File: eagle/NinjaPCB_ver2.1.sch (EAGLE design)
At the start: 58 parts, among them IC3 ANALOGSW_AD_SOT23-6, IC6 NAU7802, J2 ATX24, J3 HEATER, J4 HEATER_TEMP, Q1 S8550, Q2 IRF520NPBF, Q3 IRF520NPBF, Q4 S8550, Q5 IRF520NPBF, Q6 S8550, Q7 S8550, Q8 S8550, U1 CJT1117-3.3-SOT223

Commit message: set default 4x4
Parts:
- removed C7: CAP_SMDAL_1000UF_25V, Seeed-OPL-2017-01-Capacitor-akita:CAP_SMDAL_1000UF_25V
- removed ESP1: ESP-12F, Seeed-OPL-2017-01-Sensor-camilo:ESP-12F
- removed ESP2: ESP-WROOM-02-BREAK, PCR-Module:ESP-WROOM-02-BREAK
- removed IC3: ANALOGSW_AD_SOT23-6, PCR-IC:ANALOGSW_AD_SOT23-6
- removed IC6: NAU7802, PCR-IC:NAU7802
- removed J2: ATX24, PCR-Connector:ATX24
- removed J4: HEATER_TEMP, Seeed-Connector:SCREW-TERMINAL-GREEN(2P-3.5)
- removed JP2: 22-23-2031, con-molex:22-23-2031
- removed PWR: (no value), pinhead:PINHD-1X2
- removed Q7, Q8: S8550, Seeed-Transistor:SMD-TRANSISTORS-PNP-25V-500MA-S8550(SOT-23)
- removed R20: 100K 1/10W, Seeed-Resistor:SMD-RES-100K-5%-1/10W(0603)
- removed R22: 10K 1/10W, Seeed-Resistor:SMD-RES-10K-5%-1/10W(0603)
- removed RH1, RH2, RL: 30K HP, PCR-RCL:R0603
- removed SERIAL: (no value), pinhead:PINHD-1X6
- removed U1: CJT1117-3.3-SOT223, Seeed-IC:PMIC-CJT1117-3.3(SOT223)
- added ATX: ATX24NH, PCR-Connector:ATX24NH
- added C4: 22uf, Seeed-Capacitor:TANTALUM-SMD-22UF-16V(AVX-B)
- added CP1, CP2: 100nf, Seeed-Capacitor:CERAMIC-100NF-50V-10%-X7R(0603)
- added ESP-12: ESP-12F, Seeed-OPL-2017-01-Sensor-camilo:ESP-12F
- added ESP-WROOM-02: ESP-WROOM-02, PCR-Module:ESP-WROOM-02
- added ESP-WROOM-02-BREAK: ESP-WROOM-02-BREAKND, PCR-Module:ESP-WROOM-02-BREAKND
- added FAN: 22-23-2031, con-molex:22-23-2031
- added HEATER_TEMP: (no value), Seeed-Connector:SCREW-TERMINAL-GREEN(2P-3.5)
- added HEATSINK: HEAT111PB015, PCR-Connector:HEAT111PB015
- added IC1: ANALOGSW_AD_SOT23-6, PCR-IC:ANALOGSW_AD_SOT23-6
- added IC2: NAU7802, PCR-IC:NAU7802
- added R6: 10K 1/10W, Seeed-Resistor:SMD-RES-10K-5%-1/10W(0603)
- added REG: CJT1117-3.3-SOT223, Seeed-IC:PMIC-CJT1117-3.3(SOT223)
- added RH, RL1, RL2: 15K HP, PCR-RCL:R0603
- added RT: 5K HP, Seeed-Resistor:SMD-RES-2K-1%-1/10W(0603)
- added SERIAL4: (no value), pinhead:PINHD-1X4
- added SERIAL6: (no value), pinhead:PINHD-1X6
- added T1, T2, T3, T4, T5, T6, T7: TPTP20R, testpad:TPTP20R
- added U$10, U$3, U$4, U$5, U$6, U$7, U$8, U$9: FIDUCIAL, adafruit:FIDUCIAL
- C3: value 100nf -> CAP_SMDAL_1000UF_25V; device Seeed-Capacitor:CERAMIC-100NF-50V-10%-X7R(0603) -> Seeed-OPL-2017-01-Capacitor-akita:CAP_SMDAL_1000UF_25V
- HEATER_POWER: value HEATER -> (none)
- JACK: value 2.1MMJACKTHM -> 2.1MMJACKTHM-NOOUT; device adafruit:2.1MMJACKTHM -> adafruit:2.1MMJACKTHM-NOOUT
- Q1: value S8550 -> IRLB3813PBF; device Seeed-Transistor:SMD-TRANSISTORS-PNP-25V-500MA-S8550(SOT-23) -> transistor-power:IRF520
- Q2, Q3: value IRF520NPBF -> CJ2302; device Seeed-Transistor:DIP-MOSFET-N-CH-100V-9.7A-IRF520NPBF(TO-220AB)CORRECT -> Seeed-Transistor:SMD-MOSFET-N-CH-20V-2.1A-CJ2302(SOT-23)
- Q4, Q6: value S8550 -> S9013; device Seeed-Transistor:SMD-TRANSISTORS-PNP-25V-500MA-S8550(SOT-23) -> Seeed-Transistor:SMD-TRANSISTORS-NPN-25V-500MA-S9013(SOT-23)
- Q5: value IRF520NPBF -> S9013; device Seeed-Transistor:DIP-MOSFET-N-CH-100V-9.7A-IRF520NPBF(TO-220AB)CORRECT -> Seeed-Transistor:SMD-TRANSISTORS-NPN-25V-500MA-S9013(SOT-23)
- R12, R15, R19: value 10K 1/10W -> 1K 1/10W; device Seeed-Resistor:SMD-RES-10K-5%-1/10W(0603) -> Seeed-Resistor:SMD-RES-1K-5%-1/10W(0603)
- R13: value 100K 1/10W -> 10K 1/10W; device Seeed-Resistor:SMD-RES-100K-5%-1/10W(0603) -> Seeed-Resistor:SMD-RES-10K-5%-1/10W(0603)
- R14: value 15KHP -> 10K 1/10W; device Seeed-Resistor:SMD-RES-2K-1%-1/10W(0603) -> Seeed-Resistor:SMD-RES-10K-5%-1/10W(0603)
- R17: value 100K 1/10W -> 1K 1/10W; device Seeed-Resistor:SMD-RES-100K-5%-1/10W(0603) -> Seeed-Resistor:SMD-RES-1K-5%-1/10W(0603)
- RD1, RD2: value 30K HP -> 15K HP
- RELAY: value NEC-RELAY2ET2 -> NEC-RELAY2EP2; device PCR-Switch:NEC-RELAY2ET2 -> PCR-Switch:NEC-RELAY2EP2
- renumbered J3 to HEATER_POWER, R21 to R10
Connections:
- removed net N$25: Q3.G, Q4.E, R11.1, R17.2
- removed net N$29: Q1.E, Q2.G, R13.2, R8.1
- removed net N$31: Q4.B, R15.2
- removed net PWR: PWR.1, SERIAL.4
- new net MODE: ESP-12.ADC, ESP-WROOM-02-BREAK.TOUT, ESP-WROOM-02.TOUT, R9.2
- new net N$1: RL1.2, RL2.1
- new net N$8: Q3.G, R17.2, R18.2
- net 12V: now also ATX.12V_10, ATX.12V_11, C3.P$P, FAN-2.S, R13.2, REG.IN; no longer C7.P$P, J2.12V_10, J2.12V_11, JP2-2.S, R11.2, R19.2, R8.2, U1.IN
- net 3V3: now also C4.+, CP1.1, CP2.2, ESP-12.VCC, ESP-WROOM-02-BREAK.3V3, ESP-WROOM-02.3V3, HEATER_TEMP.1, IC1.D, IC1.VDD, IC2.AVDD, IC2.DVDD, IC2.REFP, R1.1, R3.1, REG.OUT, RL1.1, SERIAL4.1, SERIAL6.4, T3.TP; no longer C1.1, C2.+, ESP1.VCC, ESP2.3V3, IC3.D, IC3.VDD, IC6.AVDD, IC6.DVDD, IC6.REFP, J4.1, PWR.2, R1.2, R5.1, R9.1, RL.2, U1.OUT
- net DIVIDED: now also C2.+, IC2.VIN1N, IC2.VIN2N, RD2.1; no longer IC6.VIN1N, IC6.VIN2N, RD2.2
- net DRDY: now also ESP-12.GPIO5, ESP-WROOM-02-BREAK.IO5, ESP-WROOM-02.IO5, IC2.DRDY; no longer ESP1.GPIO5, ESP2.IO5, IC6.DRDY
- net EN: now also ESP-12.EN, ESP-WROOM-02-BREAK.EN, ESP-WROOM-02.EN, R4.2; no longer ESP1.EN, ESP2.EN, R1.1
- net FAN: now also ESP-12.GPIO0, ESP-WROOM-02-BREAK.IO0, ESP-WROOM-02.IO0, IO0.A0, IO0.A1, R17.1, R2.2, T5.TP; no longer ESP1.GPIO13, ESP2.IO13/HSPID/MOSI, R15.1, R3.2
- net GND: now also ATX.GND15, ATX.GND17, ATX.GND18, ATX.GND19, ATX.GND24, ATX.GND3, ATX.GND5, ATX.GND7, ATX.PWR_ON, C1.1, C3.P$M, C4.-, CP1.2, CP2.1, ESP-12.GND, ESP-WROOM-02-BREAK.GND13, ESP-WROOM-02-BREAK.GND18, ESP-WROOM-02-BREAK.GND9, ESP-WROOM-02.GND13, ESP-WROOM-02.GND18, ESP-WROOM-02.GND19, ESP-WROOM-02.GND9, IC1.GND, IC2.AVSS, IC2.DVSS, IC2.REFN, Q1.S, Q4.E, Q5.E, Q6.E, R14.1, R16.1, R18.1, R5.1, R6.1, R8.1, R9.1, RD2.2, REG.GND, RT.2, SERIAL4.4, SERIAL6.6, T4.TP; no longer C1.2, C3.1, C7.P$M, ESP1.GND, ESP2.GND13, ESP2.GND18, ESP2.GND9, IC3.GND, IC6.AVSS, IC6.DVSS, IC6.REFN, J2.GND15, J2.GND17, J2.GND18, J2.GND19, J2.GND24, J2.GND3, J2.GND5, J2.GND7, Q1.C, Q4.C, Q5.S, Q6.C, Q7.C, Q8.C, R12.1, R13.1, R14.2, R17.1, R20.1, R3.1, RD2.1, SERIAL.6, U1.GND
- net HEATER: now also ESP-12.GPIO15, ESP-WROOM-02-BREAK.IO15/HPSICS, ESP-WROOM-02.IO15/HPSICS, R15.1; no longer ESP1.GPIO15, ESP2.IO15/HPSICS, R16.1
- net HEATER_TEMP: now also HEATER_TEMP.2, IC2.VIN2P, RT.1; no longer IC6.VIN2P, J4.2, R14.1
- net HIGH_TEMP: now also ESP-12.GPIO16, ESP-WROOM-02-BREAK.IO16, ESP-WROOM-02.IO16, IC1.IN, R8.2, T7.TP; no longer ESP1.GPIO16, ESP2.IO16, IC3.IN, R12.2
- net N$27: now also IC1.S, RH.1; no longer IC3.S, RH1.1, RH2.1
- net N$3: now also HEATSINK.P$1, Q1.D; no longer Q5.D
- net N$30: now also R12.2, R19.1; no longer R18.2
- net N$32: now also Q2.G, R15.2; no longer Q1.B
- net N$33: now also Q4.C; no longer Q7.E
- net N$34: now also Q4.B; no longer Q7.B
- net N$35: now also Q5.B, R11.1; no longer Q8.B, R22.1
- net N$36: now also Q5.C; no longer Q8.E
- net N$4: now also FAN-3.S; no longer JP2-3.S
- net N$5: now also Q1.G, Q6.C, R13.1, R14.2, R19.2; no longer Q5.G, Q6.E, R19.1, R20.2
- net N$92: now also C1.2, IC2.VBG; no longer C3.2, IC6.VBG
- net PEL_PWM: now also ESP-12.GPIO4, ESP-WROOM-02-BREAK.IO4, ESP-WROOM-02.IO4, R12.1; no longer ESP1.GPIO4, ESP2.IO4, R18.1
- net PEL_SWA: now also ESP-12.GPIO12, ESP-WROOM-02-BREAK.IO12/HSPIQ/MISO, ESP-WROOM-02.IO12/HSPIQ/MISO, R5.2; no longer ESP1.GPIO12, ESP2.IO12/HSPIQ/MISO, R2.2
- net PEL_SWB: now also ESP-12.GPIO13, ESP-WROOM-02-BREAK.IO13/HSPID/MOSI, ESP-WROOM-02.IO13/HSPID/MOSI, R11.2, R6.2; no longer ESP1.GPIO0, ESP2.IO0, IO0.A0, IO0.A1, R22.2, R4.2
- net RESET: now also ESP-12.RST, ESP-WROOM-02-BREAK.RST, ESP-WROOM-02.RST, R1.2, T6.TP; no longer ESP1.RST, ESP2.RST, R9.2
- net RXD: now also ESP-12.RXD, ESP-WROOM-02-BREAK.RXD, ESP-WROOM-02.RXD, SERIAL4.2, SERIAL6.3, T2.TP; no longer ESP1.RXD, ESP2.RXD, SERIAL.3
- net SCLK: now also ESP-12.GPIO14, ESP-WROOM-02-BREAK.IO14/HSPICLK, ESP-WROOM-02.IO14/HSPICLK, IC2.SCLK; no longer ESP1.GPIO14, ESP2.IO14/HSPICLK, IC6.SCLK
- net SDIO: now also ESP-12.GPIO2, ESP-WROOM-02-BREAK.IO2, ESP-WROOM-02.IO2, IC2.SDIO, R3.2; no longer ESP1.GPIO2, ESP2.IO2, IC6.SDIO, R5.2
- net TXD: now also ESP-12.TXD, ESP-WROOM-02-BREAK.TXD, ESP-WROOM-02.TXD, SERIAL4.3, SERIAL6.2, T1.TP; no longer ESP1.TXD, ESP2.TXD, SERIAL.2
- net WELL_TEMP: now also IC2.VIN1P, RH.2, RL2.2; no longer IC6.VIN1P, RH1.2, RH2.2, RL.1
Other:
- note added: "CONFIG"
- note added: "Diff from ver2.0: 1. ATX:POWER_ON is connected to GND so that ATX works 2. Add R19 in case ESP can drive MOSFET directly. 3. FAN_ON jumper removed. it should be turn off while heating"
- note added: "Notes for wiring: 1. Don't forget to use 2oz dru. 10mil spacing is required. 2. Put OSH logo clearly 3. Put heater&its temp sensor top of board. they aren't enough long. Placing heater between relay and temp sensor may work."
- note removed: "Diff from ver2-170831: 1. Pullup IO0 2. Pulldown HEATER 3. Killed ADC MCP 4. INT_ADC is moved to HEATER_TEMP 5. RX/TX replaced 6. Use ESP-WROOM-02-BREAK 7. Use Relay instead of Motor Driver 8. NPN->PNP 9. Pullup PEL_SWA 10. Pulldown FAN 11. R between EN and 3V3 12. Pullup IO2 13. Pass cap for ESP"
- note removed: "NOTES: 1. (Rl, Rh) = IDEAL(30k, 15k), SOLDERED(20k, 10k)"
- moved on the sheet: C1, C2, IO0, JACK, MODE, Q2, Q3, Q4, R1, R11, R12, R13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

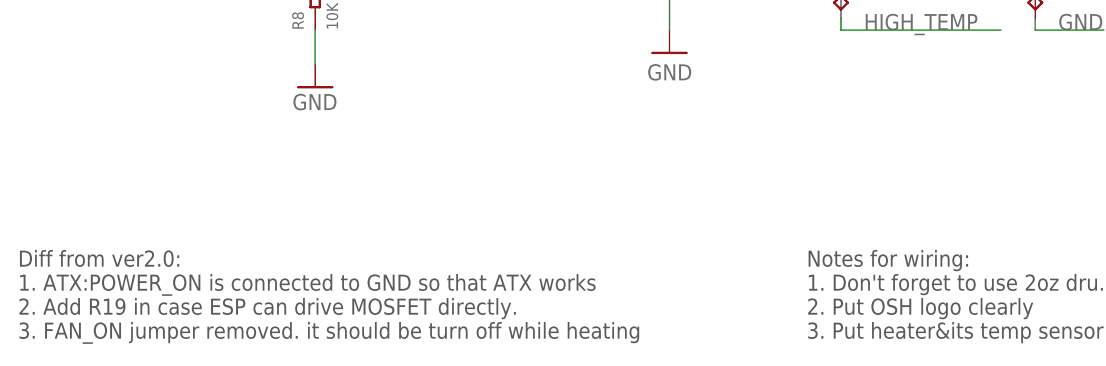
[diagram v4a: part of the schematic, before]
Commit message: remove wrong schematics
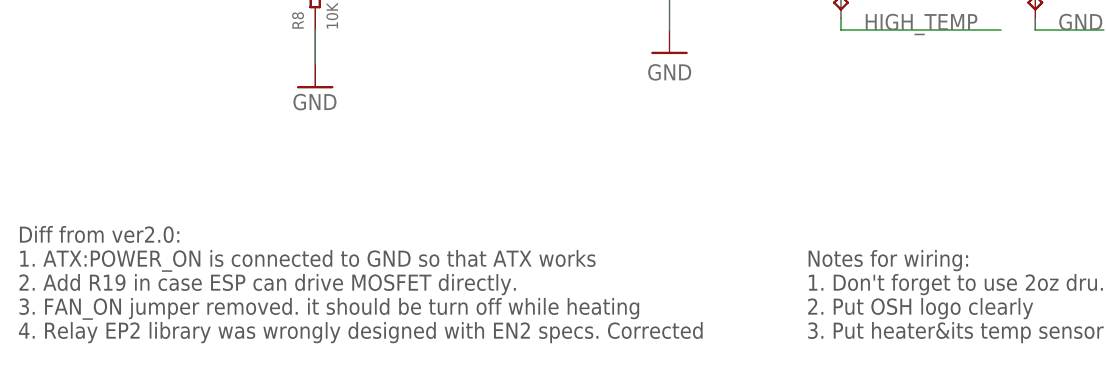
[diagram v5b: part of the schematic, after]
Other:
- note added: "Diff from ver2.0: 1. ATX:POWER_ON is connected to GND so that ATX works 2. Add R19 in case ESP can drive MOSFET directly. 3. FAN_ON jumper removed. it should be turn off while heating 4. Relay EP2 library was wrongly designed with EN2 specs. Corrected"
- note removed: "Diff from ver2.0: 1. ATX:POWER_ON is connected to GND so that ATX works 2. Add R19 in case ESP can drive MOSFET directly. 3. FAN_ON jumper removed. it should be turn off while heating"
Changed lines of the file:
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@@
 <setting verticaltext="up"/>
 </settings>
-<grid distance="0.05" unitdist="inch" unit="inch" style="lines" multiple="1" display="no" altdistance="0.01" altunitdist="inch" altunit="inch"/>
+<grid distance="0.1" unitdist="inch" unit="inch" style="lines" multiple="1" display="no" altdistance="0.01" altunitdist="inch" altunit="inch"/>
 <layers>
-<layer number="1" name="Top" color="4" fill="1" visible="no" active="no"/>
-<layer number="2" name="Route2" color="1" fill="3" visible="no" active="no"/>
-<layer number="3" name="Route3" color="4" fill="3" visible="no" active="no"/>
-<layer number="4" name="Route4" color="1" fill="4" visible="no" active="no"/>
-<layer number="5" name="Route5" color="4" fill="4" visible="no" active="no"/>
-<layer number="6" name="Route6" color="1" fill="8" visible="no" active="no"/>
-<layer number="7" name="Route7" color="4" fill="8" visible="no" active="no"/>
-<layer number="8" name="Route8" color="1" fill="2" visible="no" active="no"/>
-<layer number="9" name="Route9" color="4" fill="2" visible="no" active="no"/>
-<layer number="10" name="Route10" color="1" fill="7" visible="no" active="no"/>
-<layer number="11" name="Route11" color="4" fill="7" visible="no" active="no"/>
-<layer number="12" name="Route12" color="1" fill="5" visible="no" active="no"/>
-<layer number="13" name="Route13" color="4" fill="5" visible="no" active="no"/>
-<layer number="14" name="Route14" color="1" fill="6" visible="no" active="no"/>
-<layer number="15" name="Route15" color="4" fill="6" visible="no" active="no"/>
-<layer number="16" name="Bottom" color="1" fill="1" visible="no" active="no"/>
-<layer number="17" name="Pads" color="2" fill="1" visible="no" active="no"/>
-<layer number="18" name="Vias" color="2" fill="1" visible="no" active="no"/>
-<layer number="19" name="Unrouted" color="6" fill="1" visible="no" active="no"/>
-<layer number="20" name="Dimension" color="15" fill="1" visible="no" active="no"/>
-<layer number="21" name="tPlace" color="7" fill="1" visible="no" active="no"/>
-<layer number="22" name="bPlace" color="7" fill="1" visible="no" active="no"/>
-<layer number="23" name="tOrigins" color="15" fill="1" visible="no" active="no"/>
-<layer number="24" name="bOrigins" color="15" fill="1" visible="no" active="no"/>
-<layer number="25" name="tNames" color="7" fill="1" visible="no" active="no"/>
-<layer number="26" name="bNames" color="7" fill="1" visible="no" active="no"/>
-<layer number="27" name="tValues" color="7" fill="1" visible="no" active="no"/>
-<layer number="28" name="bValues" color="7" fill="1" visible="no" active="no"/>
+<layer number="1" name="Top" color="4" fill="1" visible="yes" active="no"/>
+<layer number="2" name="Route2" color="1" fill="3" visible="yes" active="no"/>
+<layer number="3" name="Route3" color="4" fill="3" visible="yes" active="no"/>
+<layer number="4" name="Route4" color="1" fill="4" visible="yes" active="no"/>
+<layer number="5" name="Route5" color="4" fill="4" visible="yes" active="no"/>
+<layer number="6" name="Route6" color="1" fill="8" visible="yes" active="no"/>
+<layer number="7" name="Route7" color="4" fill="8" visible="yes" active="no"/>
+<layer number="8" name="Route8" color="1" fill="2" visible="yes" active="no"/>
+<layer number="9" name="Route9" color="4" fill="2" visible="yes" active="no"/>
+<layer number="10" name="Route10" color="1" fill="7" visible="yes" active="no"/>
+<layer number="11" name="Route11" color="4" fill="7" visible="yes" active="no"/>
+<layer number="12" name="Route12" color="1" fill="5" visible="yes" active="no"/>
+<layer number="13" name="Route13" color="4" fill="5" visible="yes" active="no"/>
+<layer number="14" name="Route14" color="1" fill="6" visible="yes" active="no"/>
+<layer number="15" name="Route15" color="4" fill="6" visible="yes" active="no"/>
+<layer number="16" name="Bottom" color="1" fill="1" visible="yes" active="no"/>
+<layer number="17" name="Pads" color="2" fill="1" visible="yes" active="no"/>
+<layer number="18" name="Vias" color="2" fill="1" visible="yes" active="no"/>
+<layer number="19" name="Unrouted" color="6" fill="1" visible="yes" active="no"/>
+<layer number="20" name="Dimension" color="15" fill="1" visible="yes" active="no"/>
+<layer number="21" name="tPlace" color="7" fill="1" visible="yes" active="no"/>
+<layer number="22" name="bPlace" color="7" fill="1" visible="yes" active="no"/>
+<layer number="23" name="tOrigins" color="15" fill="1" visible="yes" active="no"/>
+<layer number="24" name="bOrigins" color="15" fill="1" visible="yes" active="no"/>
+<layer number="25" name="tNames" color="7" fill="1" visible="yes" active="no"/>
+<layer number="26" name="bNames" color="7" fill="1" visible="yes" active="no"/>
+<layer number="27" name="tValues" color="7" fill="1" visible="yes" active="no"/>
+<layer number="28" name="bValues" color="7" fill="1" visible="yes" active="no"/>
 <layer number="29" name="tStop" color="7" fill="3" visible="no" active="no"/>
 <layer number="30" name="bStop" color="7" fill="6" visible="no" active="no"/>
@@
 <layer number="35" name="tGlue" color="7" fill="4" visible="no" active="no"/>
 <layer number="36" name="bGlue" color="7" fill="5" visible="no" active="no"/>
-<layer number="37" name="tTest" color="7" fill="1" visible="no" active="no"/>
-<layer number="38" name="bTest" color="7" fill="1" visible="no" active="no"/>
+<layer number="37" name="tTest" color="7" fill="1" visible="yes" active="no"/>
+<layer number="38" name="bTest" color="7" fill="1" visible="yes" active="no"/>
 <layer number="39" name="tKeepout" color="4" fill="11" visible="no" active="no"/>
 <layer number="40" name="bKeepout" color="1" fill="11" visible="no" active="no"/>
@@
 <layer number="44" name="Drills" color="7" fill="1" visible="no" active="no"/>
 <layer number="45" name="Holes" color="7" fill="1" visible="no" active="no"/>
-<layer number="46" name="Milling" color="3" fill="1" visible="no" active="no"/>
-<layer number="47" name="Measures" color="7" fill="1" visible="no" active="no"/>
-<layer number="48" name="Document" color="7" fill="1" visible="no" active="no"/>
-<layer number="49" name="Reference" color="7" fill="1" visible="no" active="no"/>
-<layer number="50" name="dxf" color="7" fill="1" visible="no" active="no"/>
-<layer number="51" name="tDocu" color="7" fill="1" visible="no" active="no"/>
-<layer number="52" name="bDocu" color="7" fill="1" visible="no" active="no"/>
-<layer number="53" name="tGND_GNDA" color="7" fill="9" visible="no" active="no"/>
-<layer number="54" name="bGND_GNDA" color="1" fill="9" visible="no" active="no"/>
-<layer number="56" name="wert" color="7" fill="1" visible="no" active="no"/>
-<layer number="57" name="tCAD" color="7" fill="1" visible="no" active="no"/>
-<layer number="59" name="tCarbon" color="7" fill="1" visible="no" active="no"/>
-<layer number="60" name="bCarbon" color="7" fill="1" visible="no" active="no"/>
+<layer number="46" name="Milling" color="3" fill="1" visible="yes" active="no"/>
+<layer number="47" name="Measures" color="7" fill="1" visible="yes" active="no"/>
+<layer number="48" name="Document" color="7" fill="1" visible="yes" active="no"/>
+<layer number="49" name="Reference" color="7" fill="1" visible="yes" active="no"/>
+<layer number="50" name="dxf" color="7" fill="1" visible="yes" active="no"/>
+<layer number="51" name="tDocu" color="7" fill="1" visible="yes" active="no"/>
+<layer number="52" name="bDocu" color="7" fill="1" visible="yes" active="no"/>
+<layer number="53" name="tGND_GNDA" color="7" fill="9" visible="yes" active="no"/>
+<layer number="54" name="bGND_GNDA" color="1" fill="9" visible="yes" active="no"/>
+<layer number="56" name="wert" color="7" fill="1" visible="yes" active="no"/>
+<layer number="57" name="tCAD" color="7" fill="1" visible="yes" active="no"/>
+<layer number="59" name="tCarbon" color="7" fill="1" visible="yes" active="no"/>
+<layer number="60" name="bCarbon" color="7" fill="1" visible="yes" active="no"/>
 <layer number="90" name="Modules" color="5" fill="1" visible="yes" active="yes"/>
 <layer number="91" name="Nets" color="2" fill="1" visible="yes" active="yes"/>
@@
 1. ATX:POWER_ON is connected to GND so that ATX works
 2. Add R19 in case ESP can drive MOSFET directly.
-3. FAN_ON jumper removed. it should be turn off while heating</text>
+3. FAN_ON jumper removed. it should be turn off while heating
+4. Relay EP2 library was wrongly designed with EN2 specs. Corrected</text>
 <text x="22.86" y="129.54" size="3.81" layer="97">CONFIG</text>
 <text x="88.9" y="-12.7" size="1.778" layer="97">Notes for wiring:
